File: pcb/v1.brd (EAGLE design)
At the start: 92 x 80 mm, 49 parts, among them U2 MMBT3904, U3 MMBT3904, U4 MMBT3904, U5 MMBT3904

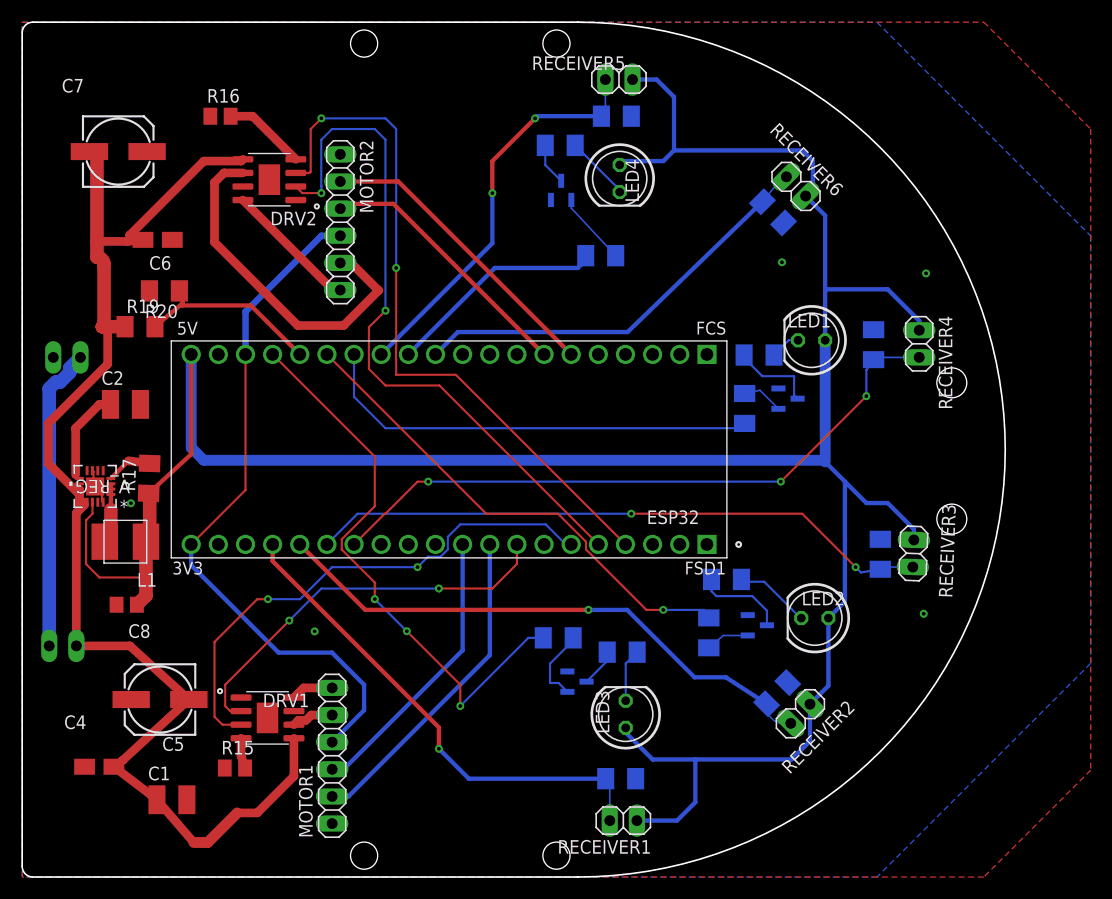
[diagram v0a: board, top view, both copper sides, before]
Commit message: Changed 5V receiver inputs to 3.3V
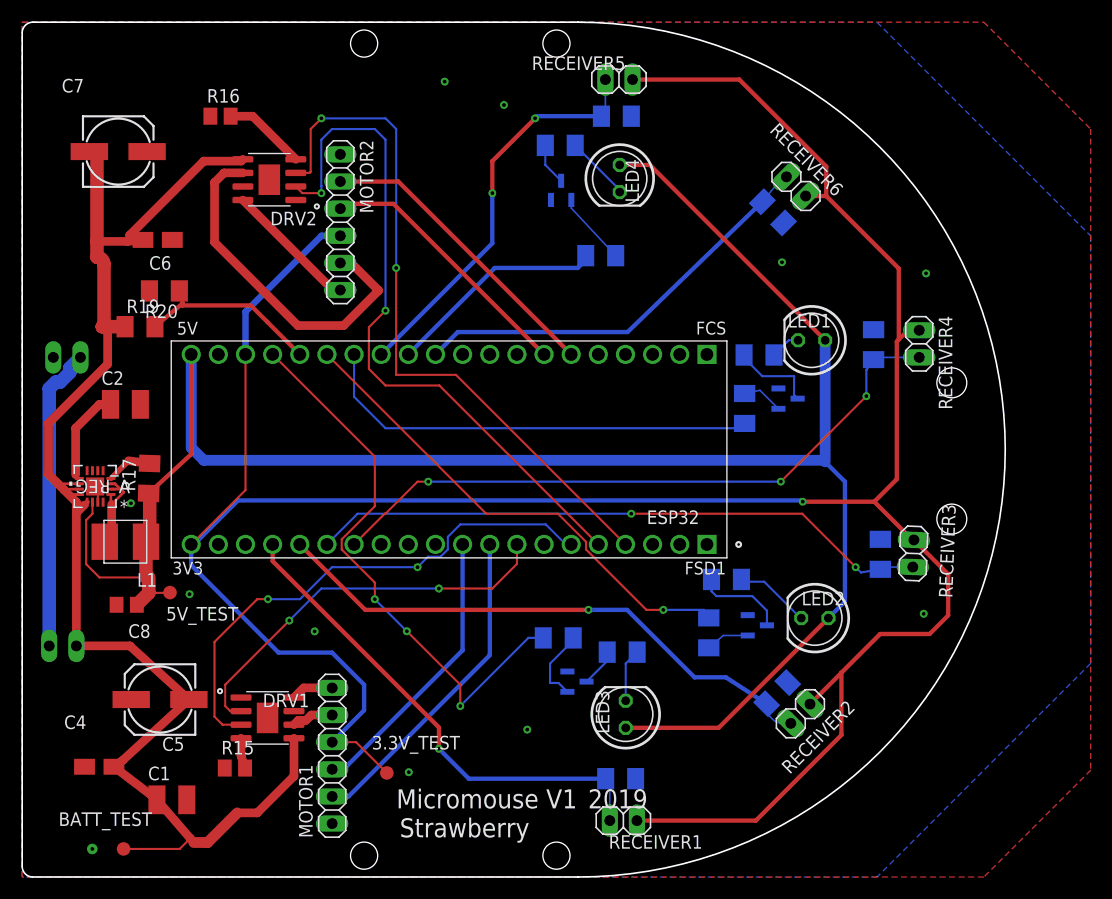
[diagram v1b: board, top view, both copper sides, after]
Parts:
- added 3.3V_TEST, 5V_TEST, BATT_TEST: PTR1B1,27, testpad:B1,27
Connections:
- net 3.3V: now also 3.3V_TEST.TP, RECEIVER1.1, RECEIVER2.1, RECEIVER3.1, RECEIVER4.1, RECEIVER5.1, RECEIVER6.1
- net 5V: now also 5V_TEST.TP; no longer RECEIVER1.1, RECEIVER2.1, RECEIVER3.1, RECEIVER4.1, RECEIVER5.1, RECEIVER6.1
- net BATT_POWER: now also BATT_TEST.TP
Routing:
- net 3.3V: track 65.1 -> 256.1 mm, vias 0 -> 1
- net 5V: track 245.7 -> 189.6 mm
- net BATT_POWER: track 123.8 -> 133.0 mm
- net N$21: track 6.10 -> 8.75 mm
- net GND: track 4.37 -> 2.69 mm
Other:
- board text added: "2019"
- board text added: "Micromouse V1"
- board text added: "Strawberry"

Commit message: Added Smd led
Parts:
- added D1, D2: APA102-5050, SparkFun-LED:APA102-5050
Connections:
- new net LED_CLK: D1.P2, ESP32.J3_8
- new net LED_SIG: D1.P1, ESP32.J3_9
- new net N$34: D1.P5, D2.P2
- new net N$35: D1.P6, D2.P1
- net 5V: now also D1.P4, D2.P4
- net GND: now also D1.P3, D2.P3
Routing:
- net LED_SIG: track 0.00 -> 43.3 mm
- net LED_CLK: track 0.00 -> 40.4 mm
- net N$34: track 0.00 -> 38.2 mm, vias 0 -> 4
- net N$35: track 0.00 -> 37.4 mm, vias 0 -> 2
- net 5V: track 189.6 -> 215.1 mm, vias 0 -> 1
- net PWM0A: vias 2 -> 1

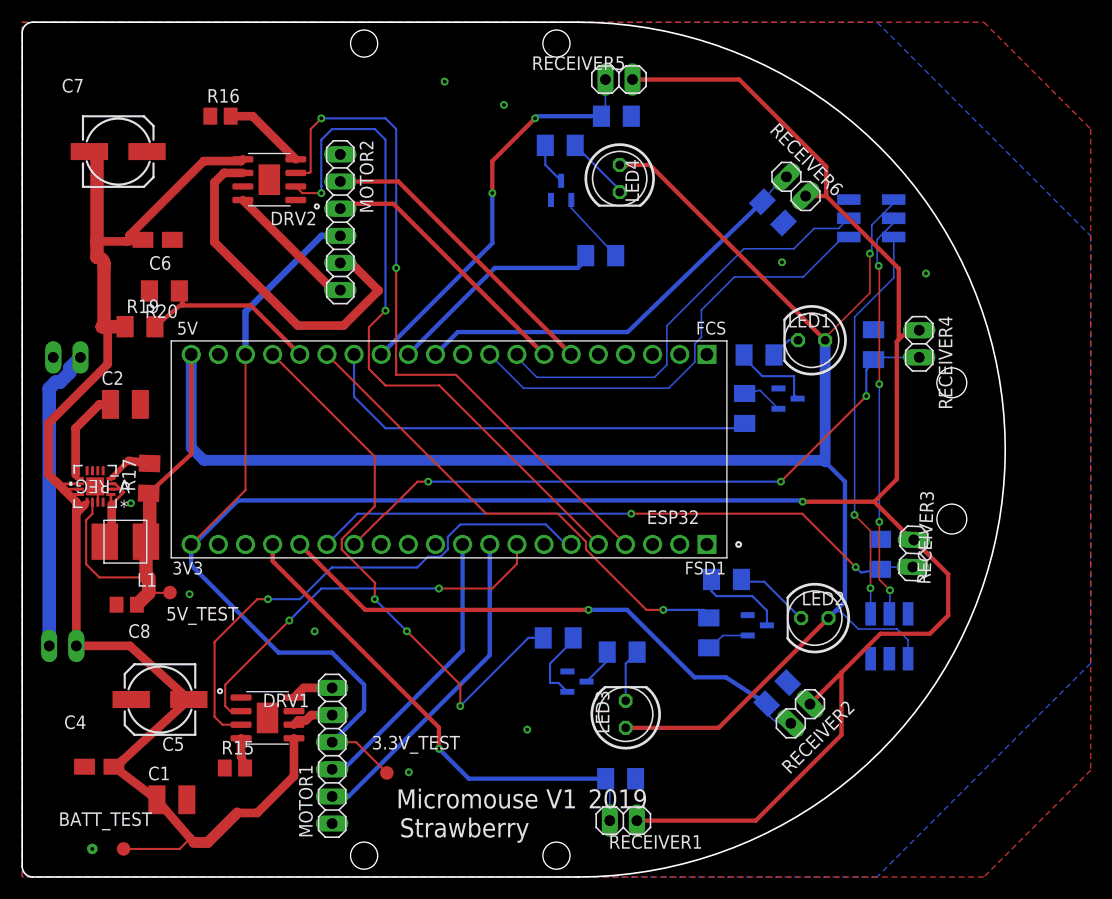
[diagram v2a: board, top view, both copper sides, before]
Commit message: Fixed led positioning and adc pins
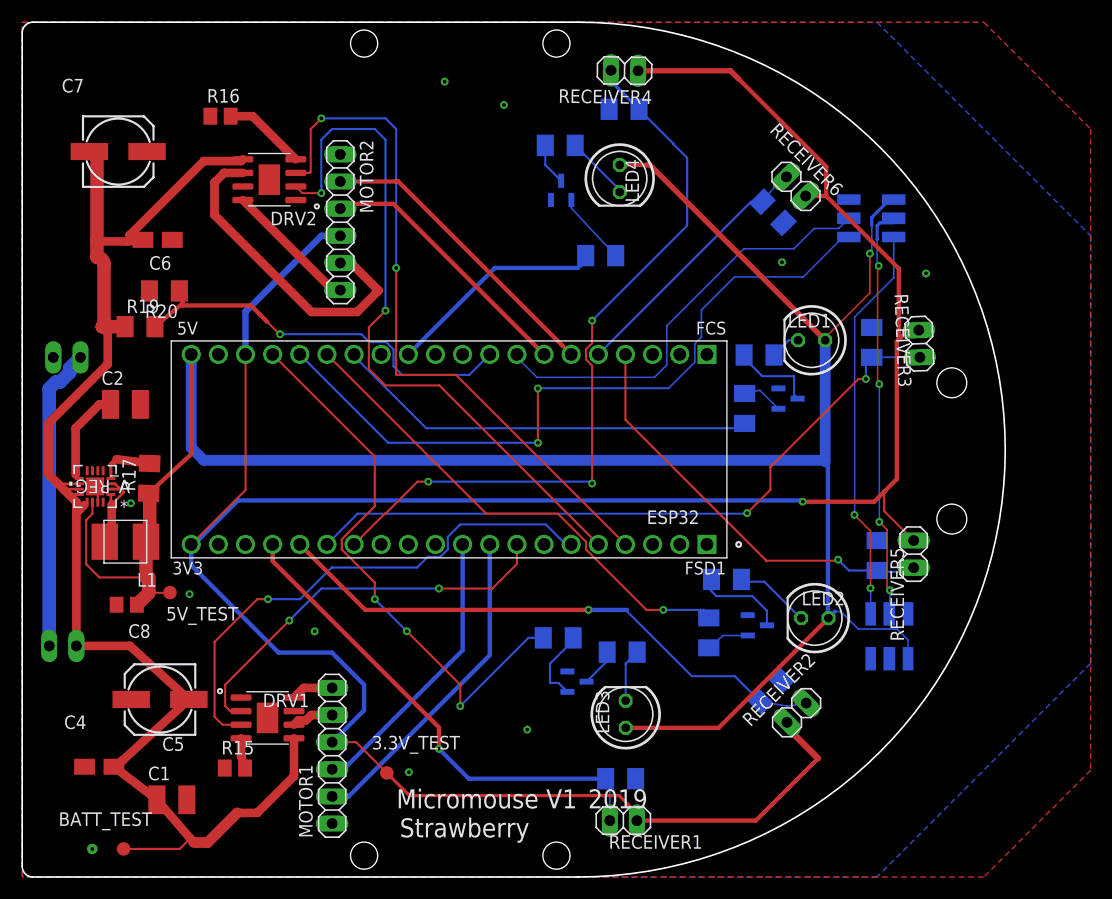
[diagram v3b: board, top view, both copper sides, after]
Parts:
- moved RECEIVER5 52.3 mm to (83.4, 30.2), turned to 270 degrees
- moved R13 47.8 mm to (80.0, 30.1), turned to 270 degrees
- moved RECEIVER4 37.6 mm to (56.4, 75.5), turned to 179.2 degrees
- moved R12 32.1 mm to (56.3, 71.9), turned to 180 degrees
- moved R11 19.8 mm to (79.5, 50.0)
- moved RECEIVER3 19.6 mm to (84.0, 49.9), turned to 272.2 degrees
- moved R10 0.69 mm to (70.0, 17.4)
- moved RECEIVER2 0.37 mm to (72.5, 15.4), turned to 45 degrees
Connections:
- net LED_SIG: now also ESP32.J3_16; no longer ESP32.J3_9
- net REC5: now also ESP32.J3_4; no longer ESP32.J3_13
- net REC6: now also ESP32.J3_5; no longer ESP32.J3_11
- net V_SENSE: now also ESP32.J3_9; no longer ESP32.J3_16
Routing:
- net LED_SIG: track 43.3 -> 68.3 mm, vias 0 -> 2
- net V_SENSE: track 17.9 -> 39.2 mm, vias 0 -> 1
- net REC6: track 39.7 -> 24.6 mm
- net REC4: track 61.6 -> 70.6 mm
- net REC3: track 58.4 -> 64.9 mm
- net 3.3V: track 256.1 -> 253.0 mm
- net N$19: track 33.2 -> 30.7 mm
- net EM1: track 41.9 -> 39.7 mm
- net 5V: track 215.1 -> 212.9 mm
- net REC5: track 37.9 -> 39.3 mm, vias 2 -> 1
- net REC2: track 52.7 -> 53.6 mm
- net N$34: track 38.2 -> 39.0 mm
- net N$22: track 4.32 -> 5.14 mm

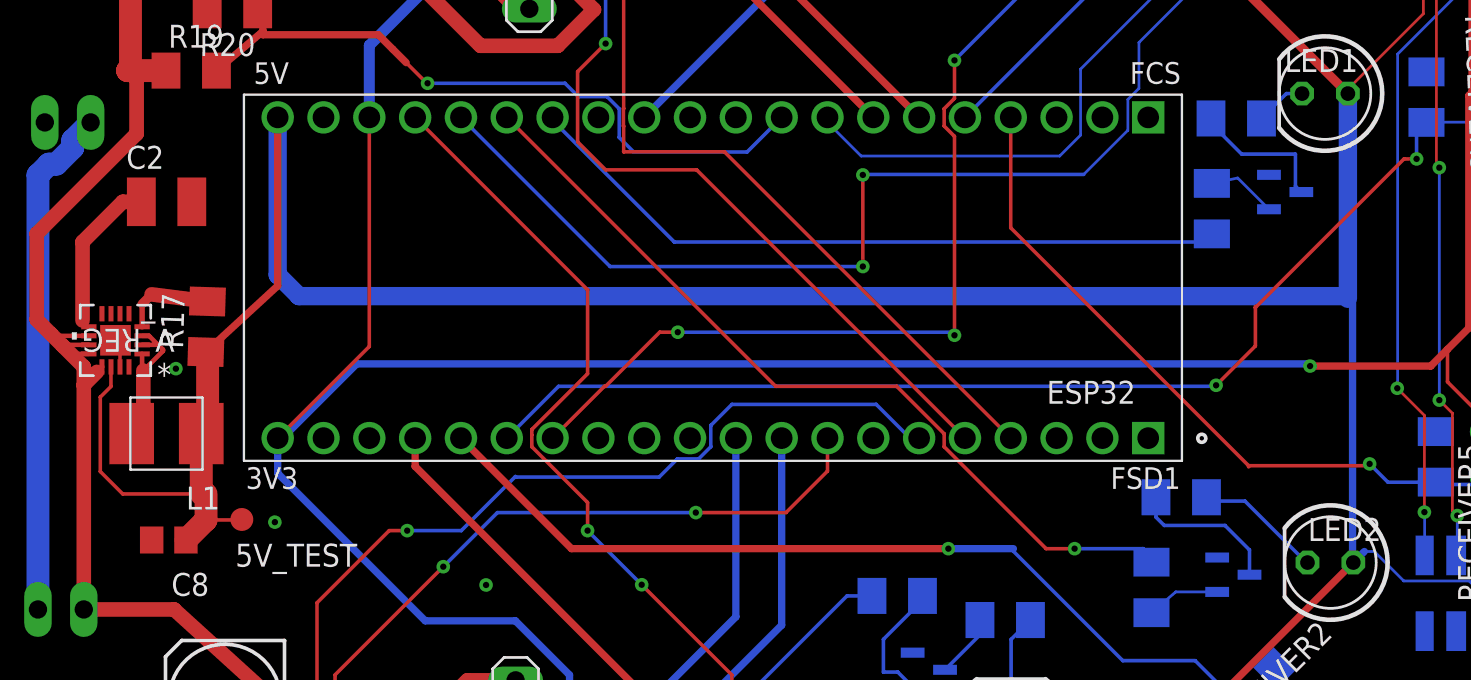
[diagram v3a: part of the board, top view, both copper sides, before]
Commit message: Changed 5V line
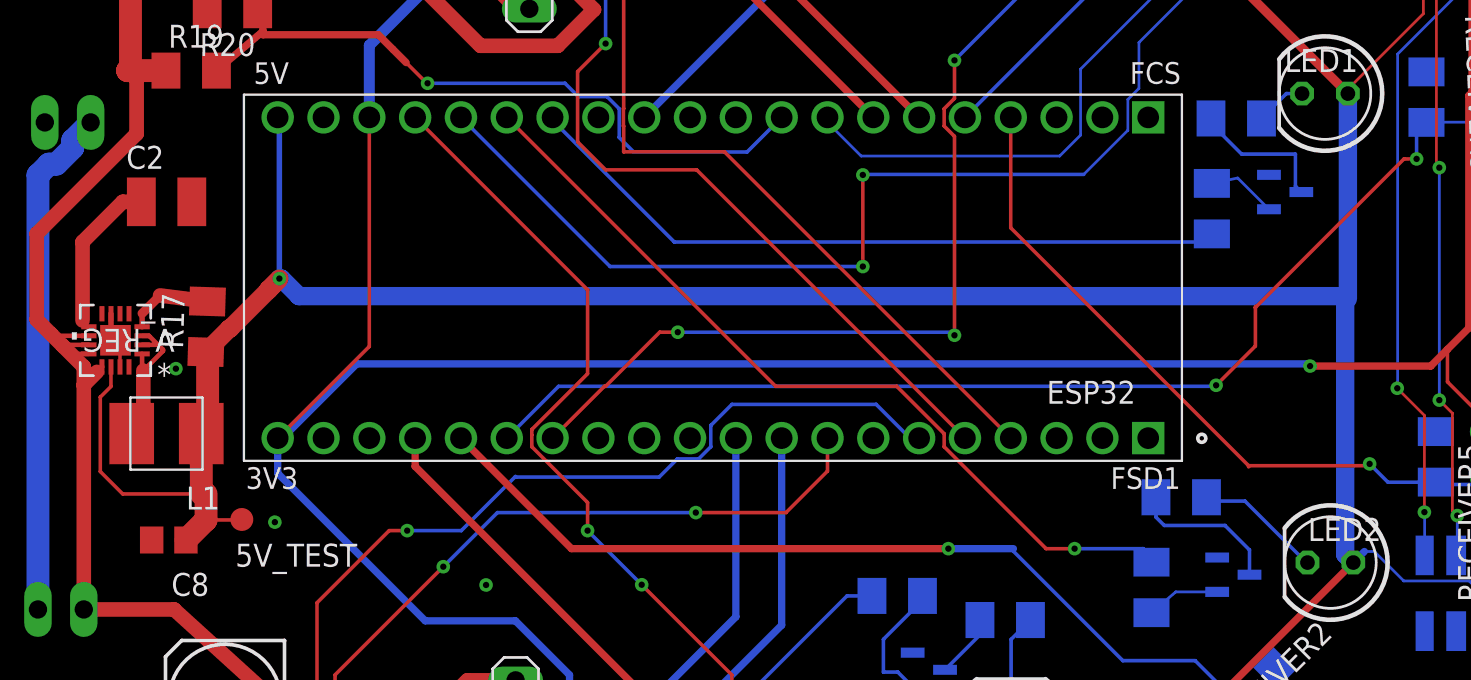
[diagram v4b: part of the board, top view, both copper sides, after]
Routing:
- net 5V: track 212.9 -> 205.4 mm, vias 1 -> 2
- net GND: track 2.69 -> 4.05 mm
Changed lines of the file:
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@@
 <setting verticaltext="up"/>
 </settings>
-<grid distance="50" unitdist="mil" unit="mm" style="lines" multiple="1" display="no" altdistance="5" altunitdist="mil" altunit="mil"/>
+<grid distance="0.003125" unitdist="mic" unit="mm" style="lines" multiple="1" display="no" altdistance="5" altunitdist="mil" altunit="mil"/>
 <layers>
 <layer number="1" name="Top" color="4" fill="1" visible="yes" active="yes"/>
@@
 <contactref element="LED3" pad="A"/>
 <contactref element="LED4" pad="A"/>
-<wire x1="11.838784375" y1="35.904040625" x2="15.8199875" y2="39.568803125" width="0.4064" layer="1"/>
-<wire x1="15.8199875" y1="39.568803125" x2="15.8199875" y2="48.90894375" width="0.4064" layer="1"/>
 <wire x1="55.56" y1="67" x2="55.92" y2="66.64" width="0.4064" layer="16"/>
 <wire x1="55.92" y1="66.64" x2="56.28" y2="67" width="0.4064" layer="16"/>
-<wire x1="75.408928125" y1="38.591071875" x2="75.408928125" y2="24.271071875" width="0.4064" layer="16"/>
 <wire x1="75.45" y1="24.23" x2="75.408928125" y2="24.271071875" width="0.4064" layer="16"/>
 <wire x1="76.062759375" y1="24.842759375" x2="75.45" y2="24.23" width="0.4064" layer="16"/>
 <wire x1="56.48" y1="13.52" x2="56.48" y2="13.96" width="0.4064" layer="16"/>
-<wire x1="15.8199875" y1="48.90894375" x2="15.8199875" y2="40.1800125" width="1.016" layer="16"/>
-<wire x1="15.8199875" y1="40.1800125" x2="17" y2="39" width="1.016" layer="16"/>
 <wire x1="75" y1="39" x2="17" y2="39" width="1.016" layer="16"/>
 <wire x1="75.15" y1="50.23" x2="75.15" y2="38.85" width="1.016" layer="16"/>
@@
 <wire x1="81.1793875" y1="63.3993875" x2="81.564015625" y2="63.3993875" width="0.3048" layer="16"/>
 <wire x1="79.51116875" y1="61.73116875" x2="81.1793875" y2="63.3993875" width="0.3048" layer="16"/>
+<wire x1="11.838784375" y1="35.904040625" x2="13.13771875" y2="37.202975" width="1.016" layer="1"/>
+<wire x1="13.13771875" y1="37.202975" x2="13.178084375" y2="37.202975" width="1.016" layer="1"/>
+<wire x1="13.178084375" y1="37.202975" x2="15.304971875" y2="39.3298625" width="1.016" layer="1"/>
+<wire x1="15.304971875" y1="39.3298625" x2="15.8199875" y2="39.844878125" width="1.016" layer="1"/>
+<wire x1="17" y1="39" x2="16.0274" y2="39.9726" width="1.016" layer="16"/>
+<wire x1="16.0274" y1="39.9726" x2="15.91233125" y2="39.9726" width="1.016" layer="16"/>
+<via x="15.91233125" y="39.9726" extent="1-16" drill="0.35"/>
+<wire x1="15.91233125" y1="39.9726" x2="15.304971875" y2="39.365240625" width="1.016" layer="1"/>
+<wire x1="15.304971875" y1="39.365240625" x2="15.304971875" y2="39.3298625" width="1.016" layer="1"/>
+<wire x1="15.91233125" y1="39.9726" x2="15.91233125" y2="48.8166" width="0.3048" layer="16"/>
+<wire x1="15.91233125" y1="48.8166" x2="15.8199875" y2="48.90894375" width="0.3048" layer="16"/>
+<wire x1="75" y1="39" x2="75" y2="24.68" width="1.016" layer="16"/>
+<wire x1="75" y1="24.68" x2="75.45" y2="24.23" width="1.016" layer="16"/>
 </signal>
 <signal name="REC1">
@@
 <wire x1="6.828084375" y1="36.549503125" x2="6.80774375" y2="36.549503125" width="0.2" layer="1"/>
 <wire x1="6.80774375" y1="36.549503125" x2="6.75" y2="36.607246875" width="0.2" layer="1"/>
-<wire x1="6.828084375" y1="36.549503125" x2="6.667346875" y2="36.710240625" width="0.1524" layer="1"/>
+<wire x1="6.667346875" y1="36.710240625" x2="6.828084375" y2="36.549503125" width="0.1524" layer="1"/>
 <contactref element="C8" pad="2"/>
 <contactref element="U3" pad="2"/>
@@
 <contactref element="D1" pad="P3"/>
 <contactref element="D2" pad="P3"/>
+<wire x1="6.578021875" y1="38.024503125" x2="6.578021875" y2="36.799565625" width="0.3048" layer="1"/>
+<wire x1="6.578021875" y1="36.799565625" x2="6.667346875" y2="36.710240625" width="0.3048" layer="1"/>
 </signal>
 <signal name="N$2">
@@
 <contactref element="V_REG" pad="4"/>
 <contactref element="R17" pad="2"/>
-<wire x1="8.83103125" y1="39.09745" x2="11.9267375" y2="38.70265625" width="0.8128" layer="1"/>
-<wire x1="8.303084375" y1="38.569503125" x2="8.83103125" y2="39.09745" width="0.508" layer="1"/>
-<wire x1="8.303084375" y1="37.299503125" x2="8.303084375" y2="38.569503125" width="0.3048" layer="1"/>
+<wire x1="9.29976875" y1="39.037671875" x2="11.9267375" y2="38.70265625" width="0.8128" layer="1"/>
+<wire x1="8.303084375" y1="38.0409875" x2="9.29976875" y2="39.037671875" width="0.508" layer="1"/>
+<wire x1="8.303084375" y1="37.299503125" x2="8.303084375" y2="38.0409875" width="0.3048" layer="1"/>
 </signal>
 <signal name="N$4">
